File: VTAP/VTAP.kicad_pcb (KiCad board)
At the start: 2 copper layers, 68 x 150 mm, 40 parts, among them J1 MX 52901-0274

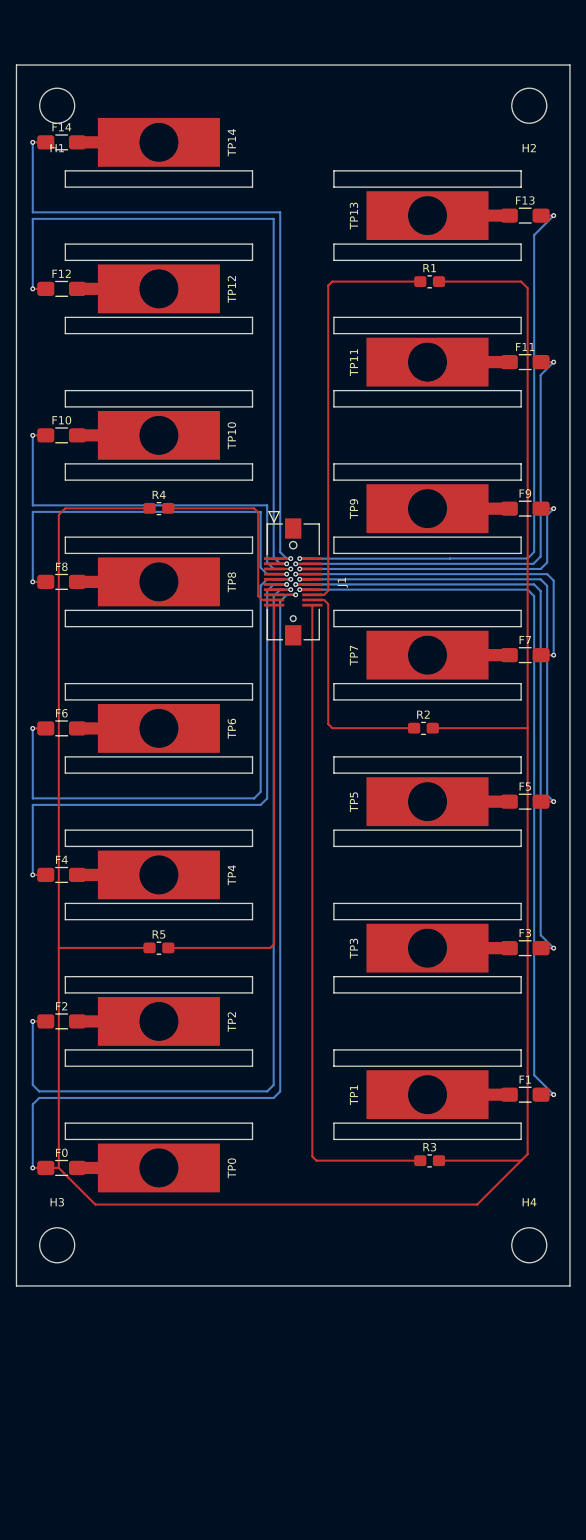
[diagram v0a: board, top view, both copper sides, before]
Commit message: fixed VTAP collisions, AMS slave redesign WIP
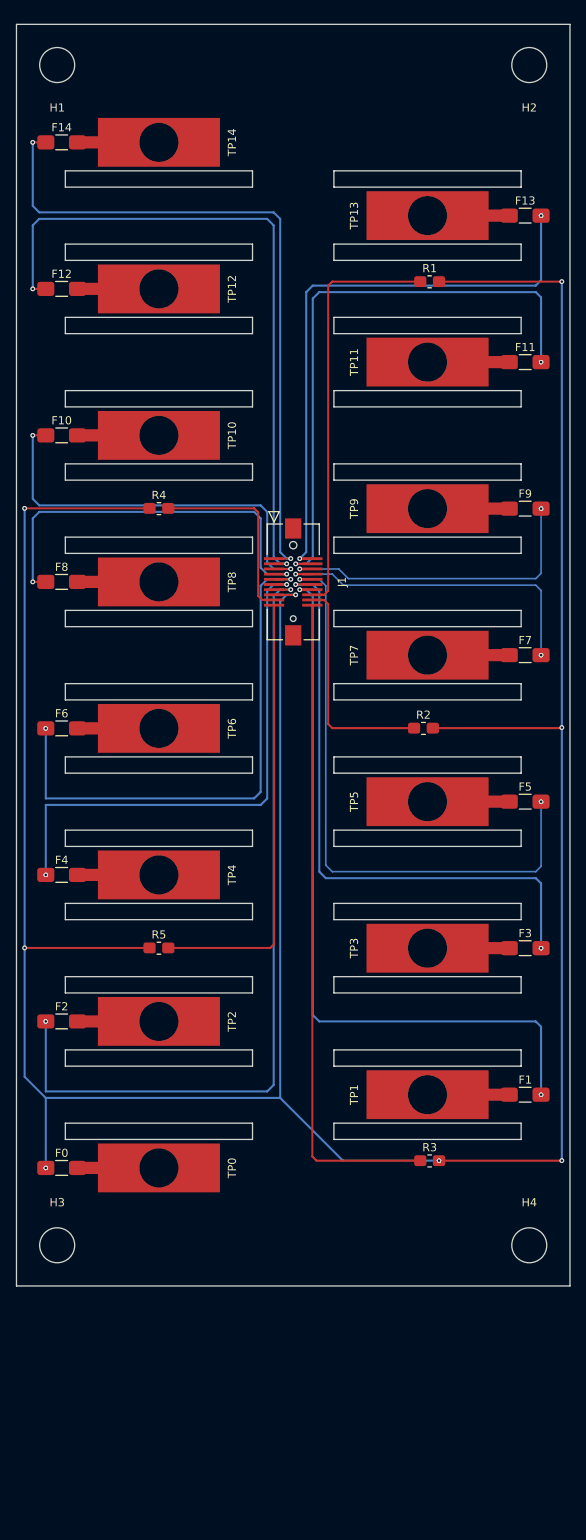
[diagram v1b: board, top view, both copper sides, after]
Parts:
- moved H1 5.00 mm to (61.0, 35.0)
- moved H2 5.00 mm to (119.0, 35.0)
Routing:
- net GND: track 411.4 -> 384.2 mm, vias 2 -> 8
- net /TP11: track 58.6 -> 72.9 mm
- net /TP5: track 60.7 -> 74.4 mm
- net /TP7: track 44.8 -> 41.0 mm
- net /TP6: track 69.9 -> 66.7 mm
- net /TP4: track 69.1 -> 65.9 mm
- net /TP3: track 78.6 -> 75.6 mm
- net /TP2: track 104.2 -> 101.5 mm
- net /TP1: track 94.5 -> 91.9 mm
- net /TP13: track 74.6 -> 72.0 mm
- net /TP10: track 51.3 -> 50.4 mm
- net /TP8: track 50.1 -> 49.2 mm
- net /TP14: track 86.0 -> 85.1 mm
- net /TP12: track 84.9 -> 83.9 mm
- net /TP9: track 40.8 -> 39.9 mm
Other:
- board size 68 x 150 mm -> 68 x 155 mm

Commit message: VTAP trace corners fixed
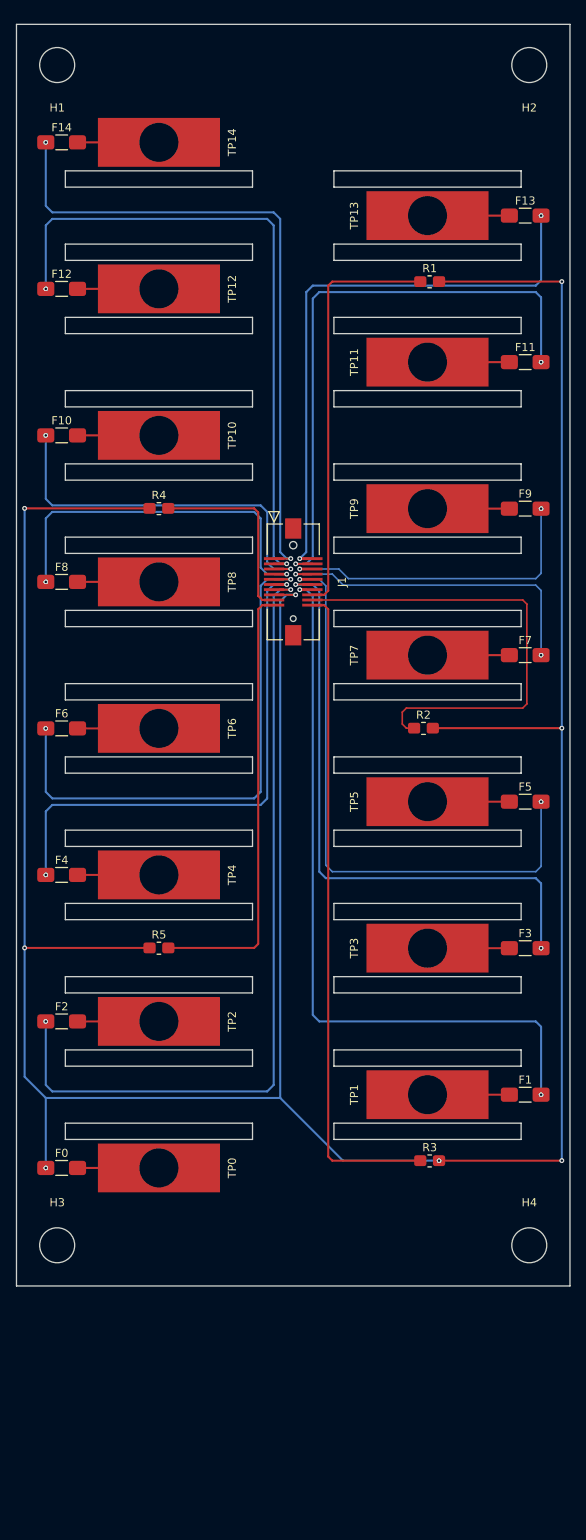
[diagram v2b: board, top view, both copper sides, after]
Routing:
- net /NTC2: track 27.7 -> 57.7 mm
- net /TP14: track 85.1 -> 81.9 mm
- net /TP8: track 49.2 -> 46.0 mm
- net /TP12: track 83.9 -> 80.7 mm
- net /TP10: track 50.4 -> 47.2 mm

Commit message: VTAP update
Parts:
- moved R2 16.8 mm to (120.2, 107.5), turned to -90 degrees
- moved R4 16.4 mm to (59.8, 80.5), turned to -90 degrees
- moved R5 16.4 mm to (59.8, 134.5), turned to -90 degrees
- moved R1 15.7 mm to (120.2, 53.5), turned to -90 degrees
- moved R3 15.7 mm to (120.2, 161.5), turned to -90 degrees
- moved F11 14.2 mm to (106.5, 63.9)
- moved F13 14.2 mm to (106.5, 61.1)
- moved F1 14.2 mm to (106.5, 169.1)
- moved F3 14.2 mm to (106.5, 135.9)
- moved F5 14.2 mm to (106.5, 133.1)
- moved F7 14.2 mm to (106.5, 99.9)
- moved F9 14.2 mm to (106.5, 97.1)
- moved F12 14.2 mm to (73.5, 54.9)
- moved F14 14.2 mm to (73.5, 52.1)
- moved F0 14.2 mm to (73.5, 162.9)
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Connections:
- F0 pad 1: GND -> Net-(F0-Pad1)
- F0 pad 2: Net-(F0-Pad2) -> GND
- F1 pad 1: Net-(F1-Pad1) -> /TP1
- F1 pad 2: /TP1 -> Net-(F1-Pad2)
- F10 pad 1: /TP10 -> Net-(F10-Pad1)
- F10 pad 2: Net-(F10-Pad2) -> /TP10
- F11 pad 1: Net-(F11-Pad1) -> /TP11
- F11 pad 2: /TP11 -> Net-(F11-Pad2)
- F12 pad 1: /TP12 -> Net-(F12-Pad1)
- F12 pad 2: Net-(F12-Pad2) -> /TP12
- F13 pad 1: Net-(F13-Pad1) -> /TP13
- F13 pad 2: /TP13 -> Net-(F13-Pad2)
- F14 pad 1: /TP14 -> Net-(F14-Pad1)
- F14 pad 2: Net-(F14-Pad2) -> /TP14
- F2 pad 1: /TP2 -> Net-(F2-Pad1)
- F2 pad 2: Net-(F2-Pad2) -> /TP2
- F3 pad 1: Net-(F3-Pad1) -> /TP3
- F3 pad 2: /TP3 -> Net-(F3-Pad2)
- F4 pad 1: /TP4 -> Net-(F4-Pad1)
- F4 pad 2: Net-(F4-Pad2) -> /TP4
- F5 pad 1: Net-(F5-Pad1) -> /TP5
- F5 pad 2: /TP5 -> Net-(F5-Pad2)
- F6 pad 1: /TP6 -> Net-(F6-Pad1)
- F6 pad 2: Net-(F6-Pad2) -> /TP6
- F7 pad 1: Net-(F7-Pad1) -> /TP7
- F7 pad 2: /TP7 -> Net-(F7-Pad2)
- F8 pad 1: /TP8 -> Net-(F8-Pad1)
- F8 pad 2: Net-(F8-Pad2) -> /TP8
- F9 pad 1: Net-(F9-Pad1) -> /TP9
- F9 pad 2: /TP9 -> Net-(F9-Pad2)
- TP0 pad 1: Net-(F0-Pad2) -> Net-(F0-Pad1)
- TP1 pad 1: Net-(F1-Pad1) -> Net-(F1-Pad2)
- TP10 pad 1: Net-(F10-Pad2) -> Net-(F10-Pad1)
- TP11 pad 1: Net-(F11-Pad1) -> Net-(F11-Pad2)
- TP12 pad 1: Net-(F12-Pad2) -> Net-(F12-Pad1)
- TP13 pad 1: Net-(F13-Pad1) -> Net-(F13-Pad2)
- TP14 pad 1: Net-(F14-Pad2) -> Net-(F14-Pad1)
- TP2 pad 1: Net-(F2-Pad2) -> Net-(F2-Pad1)
- TP3 pad 1: Net-(F3-Pad1) -> Net-(F3-Pad2)
- TP4 pad 1: Net-(F4-Pad2) -> Net-(F4-Pad1)
- TP5 pad 1: Net-(F5-Pad1) -> Net-(F5-Pad2)
- TP6 pad 1: Net-(F6-Pad2) -> Net-(F6-Pad1)
- TP7 pad 1: Net-(F7-Pad1) -> Net-(F7-Pad2)
- TP8 pad 1: Net-(F8-Pad2) -> Net-(F8-Pad1)
- TP9 pad 1: Net-(F9-Pad1) -> Net-(F9-Pad2)
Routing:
- net GND: track 384.2 -> 332.8 mm, vias 8 -> 7
- net /NTC1: track 51.2 -> 89.8 mm
- net Net-(F12-Pad1): track 0.00 -> 29.5 mm
- net Net-(F11-Pad2): track 0.00 -> 29.5 mm
- net Net-(F9-Pad2): track 0.00 -> 29.5 mm
- net Net-(F8-Pad1): track 0.00 -> 29.5 mm
- net Net-(F7-Pad2): track 0.00 -> 29.5 mm
- net Net-(F6-Pad1): track 0.00 -> 29.5 mm
- net Net-(F5-Pad2): track 0.00 -> 29.5 mm
- net Net-(F4-Pad1): track 0.00 -> 29.5 mm
- net Net-(F3-Pad2): track 0.00 -> 29.5 mm
- net Net-(F2-Pad1): track 0.00 -> 29.5 mm
- net Net-(F10-Pad1): track 0.00 -> 29.5 mm
- net Net-(F1-Pad2): track 0.00 -> 29.5 mm
- net Net-(F0-Pad1): track 0.00 -> 29.5 mm
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
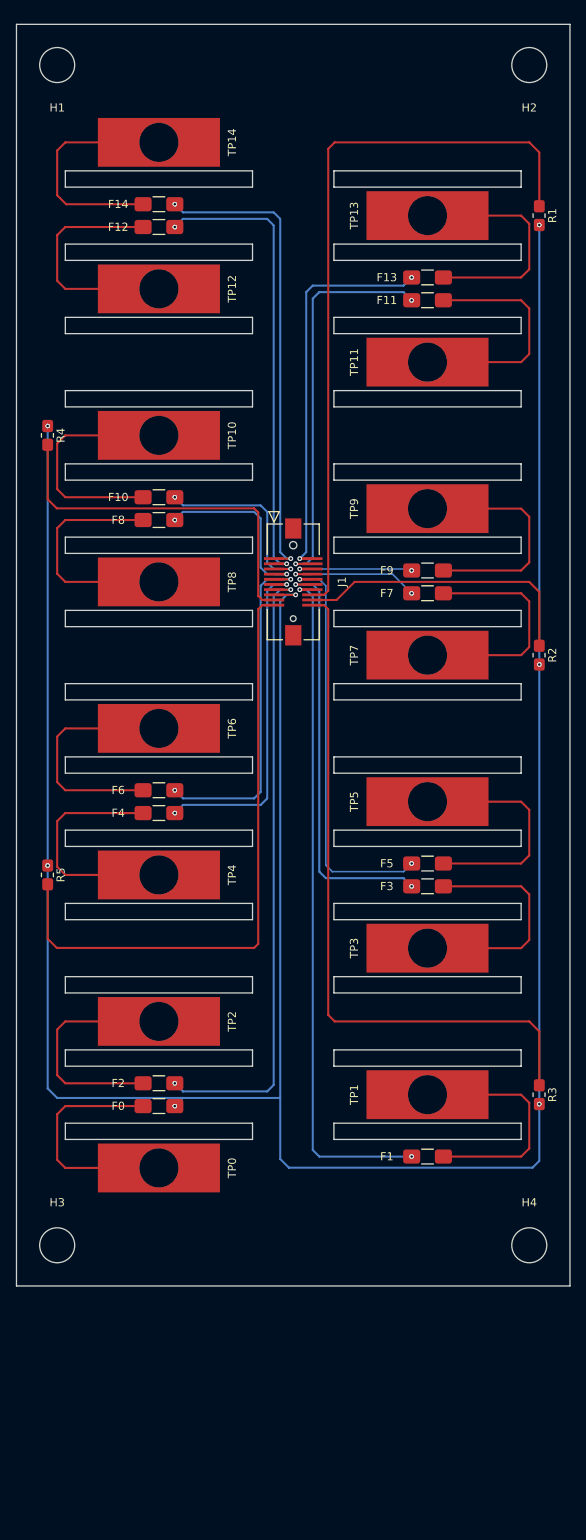
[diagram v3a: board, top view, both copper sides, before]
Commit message: fixed TS/LVS separation requirements
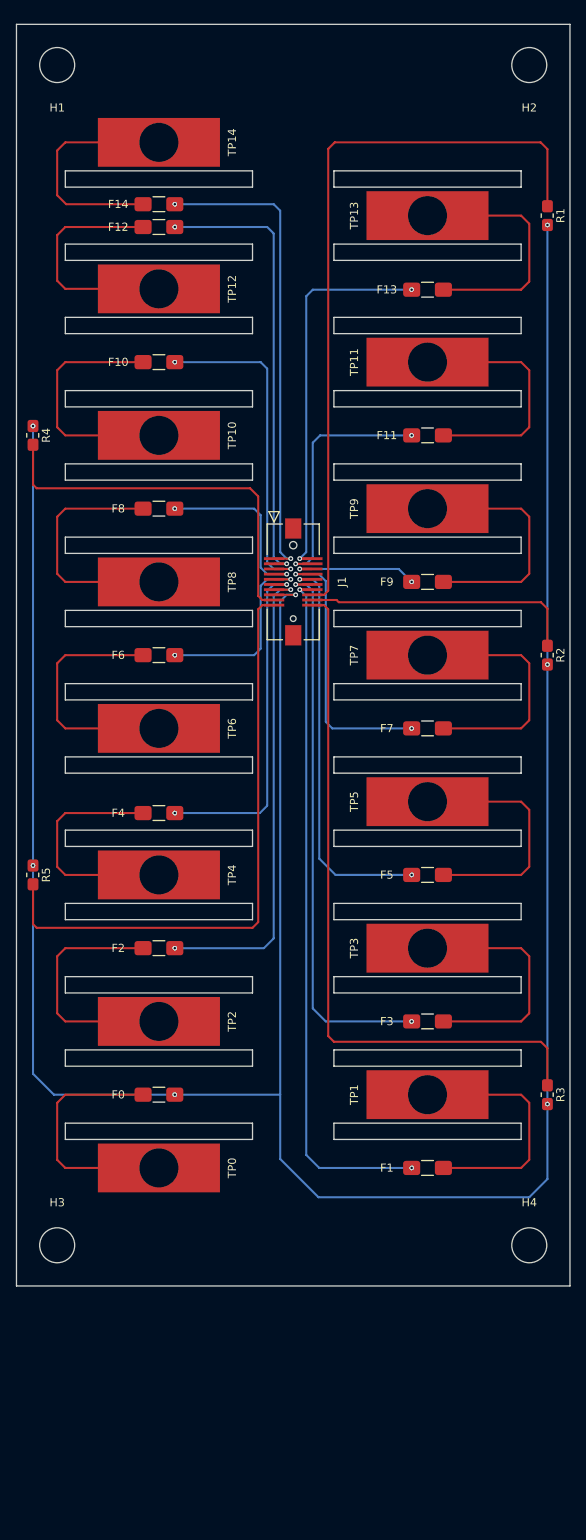
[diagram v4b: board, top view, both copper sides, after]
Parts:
- moved F11 16.6 mm to (106.5, 80.5)
- moved F10 16.6 mm to (73.5, 71.5)
- moved F2 16.6 mm to (73.5, 143.5)
- moved F3 16.6 mm to (106.5, 152.5)
- moved F6 16.6 mm to (73.5, 107.5)
- moved F7 16.6 mm to (106.5, 116.5)
- moved R4 1.80 mm to (58.0, 80.5)
- moved R5 1.80 mm to (58.0, 134.5)
- moved F13 1.50 mm to (106.5, 62.6)
- moved F0 1.40 mm to (73.5, 161.5)
- moved F1 1.40 mm to (106.5, 170.5)
- moved F5 1.40 mm to (106.5, 134.5)
- moved F8 1.40 mm to (73.5, 89.5)
- moved F9 1.40 mm to (106.5, 98.5)
- moved R1 1.00 mm to (121.2, 53.5)
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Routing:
- net /TP2: track 77.4 -> 59.2 mm
- net /TP11: track 49.2 -> 31.1 mm
- net /TP6: track 42.7 -> 24.7 mm
- net /TP10: track 23.6 -> 40.8 mm
- net /TP7: track 17.3 -> 34.3 mm
- net /TP3: track 51.9 -> 68.6 mm
- net GND: track 332.8 -> 337.3 mm
- net /NTC5: track 76.5 -> 73.6 mm
- net /NTC2: track 35.9 -> 33.9 mm
- net /NTC4: track 45.6 -> 47.5 mm
- net Net-(F13-Pad2): track 29.5 -> 31.0 mm
- net /TP12: track 57.2 -> 55.7 mm
- net Net-(F9-Pad2): track 29.5 -> 30.9 mm
- net Net-(F8-Pad1): track 29.5 -> 30.9 mm
- net Net-(F7-Pad2): track 29.5 -> 30.9 mm
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
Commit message: AMS slave schem 0.5.0 pcb 0.6.0, VTAP silkscreen
AMS slave changed to account for architectural changes
Schematic changes:
- power is now provided mainly through the 5V CAN input with voltage isolation
- BQ76940 thermistors moved to mcu
PCB changes:
- board to board connector requires all components to be on top surface
VTAP changes:
Added silkscreen to indicate cell and pack polarity
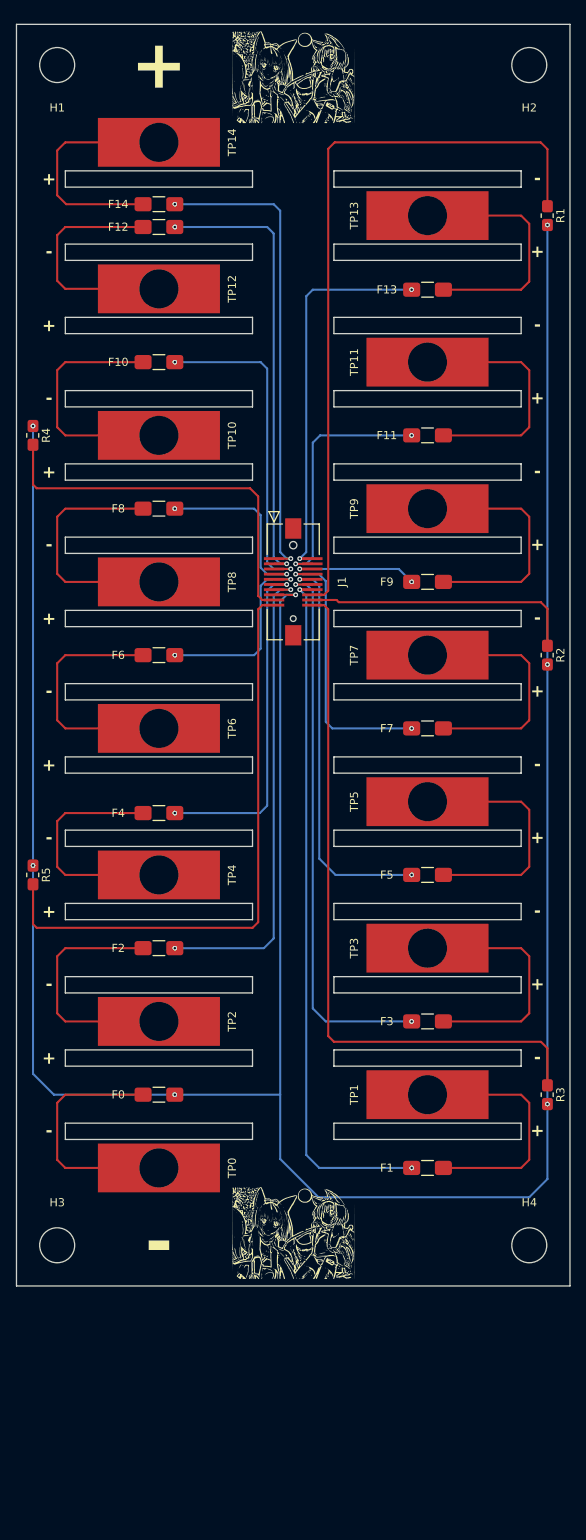
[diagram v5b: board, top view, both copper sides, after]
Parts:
- added G***: LOGO, LOGO, F.Cu at (90.0, 178.5)
- added G***: LOGO, LOGO, F.Cu at (90.0, 36.5)
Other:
- board text added: "+"
- board text added: "-"

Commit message: VTAP with new spacing
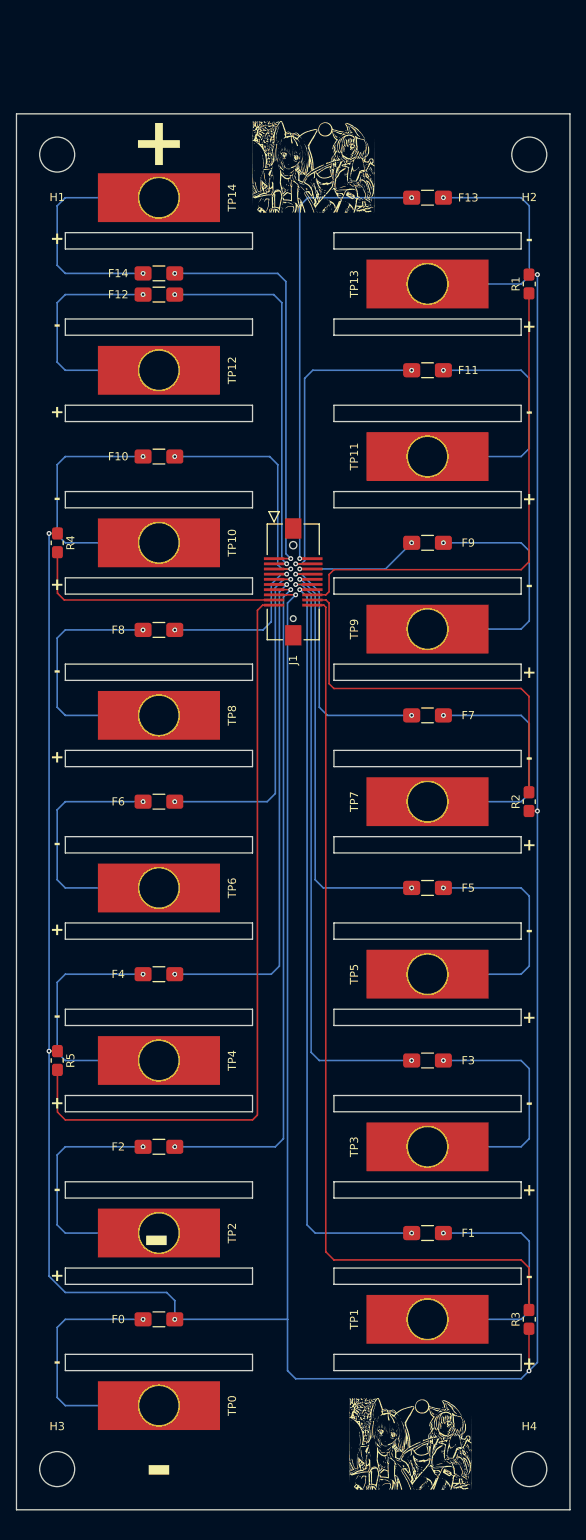
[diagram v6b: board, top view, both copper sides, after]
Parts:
- moved G*** 29.6 mm to (104.4, 204.4)
- moved TP0 29.2 mm to (73.5, 199.7)
- moved R3 27.7 mm to (119.0, 189.1), turned to 90 degrees
- moved F0 27.6 mm to (73.5, 189.1)
- moved TP1 27.6 mm to (106.5, 189.1)
- moved H3 27.5 mm to (61.0, 207.5)
- moved H4 27.5 mm to (119.0, 207.5)
- moved TP2 26.0 mm to (73.5, 178.5)
- moved F2 24.4 mm to (73.5, 167.9)
- moved TP3 24.4 mm to (106.5, 167.9)
- moved R5 23.0 mm to (61.0, 157.3)
- moved TP4 22.8 mm to (73.5, 157.3)
- moved TP5 21.2 mm to (106.5, 146.7)
- moved F4 19.8 mm to (73.5, 146.7)
- moved TP6 19.6 mm to (73.5, 136.1)
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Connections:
- F1 pad 1: /TP1 -> Net-(F1-Pad1)
- F1 pad 2: Net-(F1-Pad2) -> /TP1
- F11 pad 1: /TP11 -> Net-(F11-Pad1)
- F11 pad 2: Net-(F11-Pad2) -> /TP11
- F13 pad 1: /TP13 -> Net-(F13-Pad1)
- F13 pad 2: Net-(F13-Pad2) -> /TP13
- F3 pad 1: /TP3 -> Net-(F3-Pad1)
- F3 pad 2: Net-(F3-Pad2) -> /TP3
- F5 pad 1: /TP5 -> Net-(F5-Pad1)
- F5 pad 2: Net-(F5-Pad2) -> /TP5
- F7 pad 1: /TP7 -> Net-(F7-Pad1)
- F7 pad 2: Net-(F7-Pad2) -> /TP7
- F9 pad 1: /TP9 -> Net-(F9-Pad1)
- F9 pad 2: Net-(F9-Pad2) -> /TP9
- R2 pad 1: /NTC2 -> GND
- R2 pad 2: GND -> /NTC2
- R3 pad 1: /NTC3 -> GND
- R3 pad 2: GND -> /NTC3
- TP1 pad 1: Net-(F1-Pad2) -> Net-(F1-Pad1)
- TP11 pad 1: Net-(F11-Pad2) -> Net-(F11-Pad1)
- TP13 pad 1: Net-(F13-Pad2) -> Net-(F13-Pad1)
- TP3 pad 1: Net-(F3-Pad2) -> Net-(F3-Pad1)
- TP5 pad 1: Net-(F5-Pad2) -> Net-(F5-Pad1)
- TP7 pad 1: Net-(F7-Pad2) -> Net-(F7-Pad1)
- TP9 pad 1: Net-(F9-Pad2) -> Net-(F9-Pad1)
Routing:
- net GND: track 337.3 -> 397.4 mm
- net Net-(F13-Pad1): track 0.00 -> 32.5 mm, vias 0 -> 1
- net Net-(F9-Pad1): track 0.00 -> 32.5 mm, vias 0 -> 1
- net Net-(F7-Pad1): track 0.00 -> 32.5 mm, vias 0 -> 1
- net Net-(F5-Pad1): track 0.00 -> 32.5 mm, vias 0 -> 1
- net Net-(F3-Pad1): track 0.00 -> 32.5 mm, vias 0 -> 1
- net Net-(F11-Pad1): track 0.00 -> 32.5 mm, vias 0 -> 1
- net Net-(F1-Pad1): track 0.00 -> 32.5 mm, vias 0 -> 1
- net Net-(F13-Pad2): track 31.0 -> 0.00 mm
- net Net-(F9-Pad2): track 30.9 -> 0.00 mm
- net Net-(F7-Pad2): track 30.9 -> 0.00 mm
- net Net-(F5-Pad2): track 30.9 -> 0.00 mm
- net Net-(F3-Pad2): track 30.9 -> 0.00 mm
- net Net-(F11-Pad2): track 30.9 -> 0.00 mm
- net Net-(F1-Pad2): track 30.9 -> 0.00 mm
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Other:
- board size 68 x 155 mm -> 68 x 171.5 mm
